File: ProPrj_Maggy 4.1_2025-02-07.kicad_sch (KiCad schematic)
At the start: 102 parts, among them CN1 430451000, CN2 0430450800, U1 LM1117S-5.0, U10 TLV493DA1B6HTSA2, U11 TLV493DA1B6HTSA2, U12 TLV493DA1B6HTSA2, U13 TLV493DA1B6HTSA2, U14 TLV493DA1B6HTSA2, U15 TLV493DA1B6HTSA2, U16 TLV493DA1B6HTSA2, U17 TLV493DA1B6HTSA2, U2 LM1117S-3.3, U20 A4950ELJTR-T, U21 A4950ELJTR-T, U22 A4950ELJTR-T, U23 A4950ELJTR-T, U27 BZT52C6V2, U3 CH224K, U30 INA214AIDCKR, U31 INA214AIDCKR, U32 INA214AIDCKR, U33 INA214AIDCKR, U4 X6511FV-24-C85D32, U40 TLV2372IDR, U5 X6511FV-24-C85D32, U50 XY308-2.54-2P, U51 XY308-2.54-2P, U52 XY308-2.54-2P, U53 XY308-2.54-2P, U6 XH-4AW米色, U7 TCA9548APWR

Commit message: feat: updated schematic with replacement from I2C sensors to SPI sensors
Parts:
- removed ?: (no value), ProPrj_Mag-easyedapro:, symbol ProPrj_Mag-easyedapro:Sheet-Symbol_A4
- removed C10, C11, C12, C13, C14, C5, C7, C8, C9: 100nF, ProPrj_Maggy 4.1_2025-02-07-import-fps:C0805, symbol ProPrj_Mag-easyedapro:CAP
- removed C6: 1uF, ProPrj_Maggy 4.1_2025-02-07-import-fps:C0805, symbol ProPrj_Mag-easyedapro:CAP
- removed R1, R2: 1k2, ProPrj_Maggy 4.1_2025-02-07-import-fps:R0805, symbol ProPrj_Mag-easyedapro:Res
- removed R10, R11, R12, R13, R14, R15, R16, R17, R18, R19, R20, R21, R6, R7, R8, R9: 1k2, ProPrj_Mag-easyedapro:, symbol ProPrj_Mag-easyedapro:Res
- removed U10, U11, U12, U13, U14, U15, U16, U17: TLV493DA1B6HTSA2, ProPrj_Mag-easyedapro:, symbol ProPrj_Mag-easyedapro:TLV493DA1B6HTSA2
- removed U6: XH-4AW米色, ProPrj_Mag-easyedapro:, symbol ProPrj_Mag-easyedapro:S4B-PH-KL(LF)(SN)
- removed U7: TCA9548APWR, ProPrj_Mag-easyedapro:, symbol ProPrj_Mag-easyedapro:PCA9548APW
- added C28, C29, C30, C31, C32: 100nF, ProPrj_Maggy 4.1_2025-02-07-import-fps:C0805, symbol ProPrj_Mag-easyedapro:CAP
- added R30, R31, R41: 10K, ProPrj_Mag-easyedapro:R0805, symbol ProPrj_Mag-easyedapro:Res
- added U18, U19, U7, U8, U9: TMAG5170A2DGKR, Package_SO:VSSOP-8_3x3mm_P0.65mm, symbol Sensor_Magnetic:TMAG5170-Q1
- R32, R33, R34: value 1k2 -> 10K; footprint ProPrj_Maggy 4.1_2025-02-07-import-fps:R0805 -> ProPrj_Mag-easyedapro:R0805; Check false -> (none)
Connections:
- net 3V3: no longer R32.1, R33.1, R34.1
- net GND: now also C28.1, C29.1, C30.1, C31.1, C32.1, U18.6 (GND), U18.7 (TEST), U19.6 (GND), U19.7 (TEST), U7.6 (GND), U7.7 (TEST), U8.6 (GND), U8.7 (TEST), U9.6 (GND), U9.7 (TEST)
- net SPI_SCLK: now reaches U5.14
- net SPI_SCLK: now also U18.1 (SCLK), U19.1 (SCLK), U7.1 (SCLK), U8.1 (SCLK), U9.1 (SCLK)
- net SPI_MOSI: now reaches U4.13
- net SPI_MOSI: now also U18.2 (MOSI), U19.2 (MOSI), U7.2 (MOSI), U8.2 (MOSI), U9.2 (MOSI)
- net SPI_MISO: now reaches U4.14
- net SPI_MISO: now also U18.3 (MISO), U19.3 (MISO), U7.3 (MISO), U8.3 (MISO), U9.3 (MISO)
- net SPI_CS_4: now reaches U4.19
- net SPI_CS_4: now also R33.1, U18.4 (~{CS})
- net SPI_CS_5: now reaches U4.20
- net SPI_CS_5: now also R34.1, U19.4 (~{CS})
- net TMAG_ALERT: now reaches U4.21
- net TMAG_ALERT: now also R41.2, U18.8 (~{ALERT}), U19.8 (~{ALERT}), U7.8 (~{ALERT}), U8.8 (~{ALERT}), U9.8 (~{ALERT})
- net I2C_RST renamed SPI_CS_3
- net SPI_CS_3: now also R32.1, U9.4 (~{CS}); no longer R32.2
- net I2C_SCL: no longer names the net of U5.8
- net I2C_SCL2 renamed SPI_CS_1
- net SPI_CS_1: now also R30.1, U7.4 (~{CS}); no longer R34.2
- net I2C_SDA: no longer names the net of U5.9
- net I2C_SDA2 renamed SPI_CS_2
- net SPI_CS_2: now also R31.1, U8.4 (~{CS}); no longer R33.2
- new net +3V3: R41.1
- new net VCC: C28.2, C29.2, C30.2, C31.2, C32.2, R30.2, R31.2, R32.2, R33.2, R34.2, U18.5 (VCC), U19.5 (VCC), U7.5 (VCC), U8.5 (VCC), U9.5 (VCC)
- no-connect marks 26 -> 22
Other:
- note removed: "Mux_Sensors"
- moved on the sheet: C1, C15, C16, C17, C18, C19, C2, C20, C21, C22, C23, C24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

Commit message: chore: replace EasyEDA power symbols with KiCad power symbols
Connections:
- net 3V3 is gone; now on net +3V3: C23.2, C24.2, C25.2, C26.2, C27.1, C4.1, LED1.2 (A), R27.1, R28.2, R39.2, U2.2 (OUT), U2.4 (TAB), U20.4 (VREF), U21.4 (VREF), U22.4 (VREF), U23.4 (VREF), U3.1 (VDD), U30.3 (V+), U31.3 (V+), U32.3 (V+), U33.3 (V+), U40.8 (VDD+)
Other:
- moved on the sheet: C24, C25, R36, U31

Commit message: chore: re-annotated entire schematic
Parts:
- renumbered C27 to C1, C2 to C10, C4 to C11, C22 to C12, C18 to C13, C23 to C14, C25 to C15, C24 to C16, C26 to C17, C28 to C18, C29 to C19, C15 to C2, C30 to C20, C31 to C21, C32 to C22, C19 to C3, C16 to C4, C20 to C5, C1 to C6, C3 to C7, C21 to C8, C17 to C9, CN2 to CN1, CN1 to CN2, LED4 to LED1, LED3 to LED2, LED2 to LED3, LED1 to LED4, R29 to R1, R25 to R10, R23 to R11, R4 to R12, R3 to R13, R41 to R14, R35 to R15, R37 to R16, R36 to R17, R38 to R18, R30 to R19, R26 to R2, R31 to R20, R32 to R21, R33 to R22, R34 to R23, R27 to R3, R22 to R4, R24 to R5, R28 to R6, R5 to R7, R39 to R8, R40 to R9, U20 to U1, U21 to U10, U1 to U11, U2 to U12, U40 to U13, U4 to U14, U30 to U15, U32 to U16, U5 to U17, U31 to U18, U33 to U19, U22 to U2, U7 to U20, U8 to U21, U9 to U22, U18 to U23, U19 to U24, U27 to U4, U50 to U5, U51 to U6, U52 to U7, U53 to U8, U23 to U9

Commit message: chore: auto-placed labels, replaced easyeda yellow-green LED with KiCad LED
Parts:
- LED1: value XL-1608SYGC-06 -> Yellow-Green; footprint ProPrj_Maggy 4.1_2025-02-07-import-fps:LED0603-RD_GREEN -> LED_SMD:LED_0603_1608Metric; symbol ProPrj_Mag-easyedapro:XL-1608SYGC-06 -> Device:LED
- LED2, LED4: footprint ProPrj_Maggy 4.1_2025-02-07-import-fps:LED0603-RD_GREEN -> ProPrj_Mag-easyedapro:LED0603-RD_GREEN; symbol ProPrj_Mag-easyedapro:XL-1608SYGC-06 -> Device:LED
- LED3: footprint ProPrj_Maggy 4.1_2025-02-07-import-fps:LED0603-RD_RED -> ProPrj_Mag-easyedapro:LED0603-RD_RED; symbol ProPrj_Mag-easyedapro:XL-1608SURC-06 -> Device:LED; LCSC Part Name XL-1608SYGC-06 -> XL-1608SURC-06; Manufacturer Part XL-1608SYGC-06 -> XL-1608SURC-06; Supplier Part C965805 -> C965799
- R1, R10, R11, R12, R13, R14, R19, R2, R20, R21, R22, R23, R3, R4, R5, R6, R7, R8, R9: symbol ProPrj_Mag-easyedapro:Res -> Device:R
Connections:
- net +3V3: no longer LED4.2 (A), R14.1
- net +5V: no longer LED3.2 (A)
- net TMAG_ALERT: no longer R14.2
- net at LED4.1 (K): no longer R13.2
- net at U4.1 (C): no longer LED2.1 (K)
- net at R7.1: no longer LED2.2 (A)
- net at R12.2: no longer LED3.1 (K)

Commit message: chore: replaced all yellow-green LEDs
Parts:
- LED2, LED4: value XL-1608SYGC-06 -> Yellow-Green; footprint ProPrj_Mag-easyedapro:LED0603-RD_GREEN -> LED_SMD:LED_0603_1608Metric
- LED3: value XL-1608SYGC-06 -> Yellow-Green; footprint ProPrj_Mag-easyedapro:LED0603-RD_RED -> LED_SMD:LED_0603_1608Metric
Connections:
- net +3V3: now also LED4.2 (A), R14.1
- net +5V: now also LED3.2 (A)
- net TMAG_ALERT: now also R14.2
- net at LED4.1 (K): now also R13.2
- net at U4.1 (C): now also LED2.1 (K)
- net at R7.1: now also LED2.2 (A)
- net at R12.2: now also LED3.1 (K)
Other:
- moved on the sheet: R14
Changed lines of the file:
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@@
 	(wire
 		(pts
-			(xy 179.07 82.55) (xy 179.07 81.28)
-		)
-		(stroke
-			(width 0)
-			(type default)
-		)
-	)
-	(wire
-		(pts
 			(xy 339.09 97.79) (xy 341.63 97.79)
 		)
@@
 	(wire
 		(pts
-			(xy 179.07 71.12) (xy 179.07 69.85)
-		)
-		(stroke
-			(width 0)
-			(type default)
-		)
-	)
-	(wire
-		(pts
 			(xy 124.46 273.05) (xy 121.92 273.05)
 		)
@@
 	(wire
 		(pts
-			(xy 179.07 46.99) (xy 179.07 48.26)
+			(xy 179.07 45.72) (xy 179.07 48.26)
 		)
 		(stroke
@@
 	(wire
 		(pts
-			(xy 179.07 36.83) (xy 179.07 35.56)
+			(xy 179.07 35.56) (xy 179.07 38.1)
 		)
 		(stroke
@@
 	(wire
 		(pts
-			(xy 102.87 161.29) (xy 102.87 162.56)
+			(xy 102.87 161.29) (xy 102.87 163.83)
 		)
 		(stroke
@@
 	(wire
 		(pts
+			(xy 179.07 69.85) (xy 179.07 72.39)
+		)
+		(stroke
+			(width 0)
+			(type default)
+		)
+	)
+	(wire
+		(pts
 			(xy 335.28 240.03) (xy 336.55 240.03)
 		)
@@
 	(wire
 		(pts
-			(xy 191.77 173.99) (xy 194.31 173.99)
+			(xy 191.77 173.99) (xy 195.58 173.99)
 		)
 		(stroke
@@
 	(wire
 		(pts
+			(xy 102.87 171.45) (xy 102.87 172.72)
+		)
+		(stroke
+			(width 0)
+			(type default)
+		)
+	)
+	(wire
+		(pts
 			(xy 354.33 196.85) (xy 359.41 196.85)
 		)
@@
 	(wire
 		(pts
+			(xy 179.07 80.01) (xy 179.07 82.55)
+		)
+		(stroke
+			(width 0)
+			(type default)
+		)
+	)
+	(wire
+		(pts
 			(xy 142.24 186.69) (xy 152.4 186.69)
 		)
@@
 	(wire
 		(pts
+			(xy 203.2 173.99) (xy 204.47 173.99)
+		)
+		(stroke
+			(width 0)
+			(type default)
+		)
+	)
+	(wire
+		(pts
 			(xy 130.81 82.55) (xy 130.81 74.93)
 		)
@@
 		(at 179.07 76.2 90)
 		(unit 1)
-		(body_style 0)
+		(body_style 1)
 		(exclude_from_sim no)
 		(in_bom yes)
@@
 			)
 		)
-		(property "Value" "XL-1608SYGC-06"
+		(property "Value" "Yellow-Green"
 			(at 182.88 79.0574 90)
 			(show_name no)
@@
 			)
 		)
-		(property "Footprint" "ProPrj_Mag-easyedapro:LED0603-RD_GREEN"
+		(property "Footprint" "LED_SMD:LED_0603_1608Metric"
 			(at 179.07 76.2 0)
 			(hide yes)
@@
 			)
 		)
-		(property "Value" "XL-1608SYGC-06"
+		(property "Value" "Yellow-Green"
 			(at 106.68 170.4974 90)
 			(show_name no)
@@
 			)
 		)
-		(property "Footprint" "ProPrj_Mag-easyedapro:LED0603-RD_GREEN"
+		(property "Footprint" "LED_SMD:LED_0603_1608Metric"
 			(at 102.87 167.64 0)
 			(hide yes)
@@
 		(at 179.07 41.91 90)
 		(unit 1)
-		(body_style 0)
+		(body_style 1)
 		(exclude_from_sim no)
 		(in_bom yes)
@@
 			)
 		)
-		(property "Value" "XL-1608SYGC-06"
+		(property "Value" "Yellow-Green"
 			(at 182.88 44.7674 90)
 			(show_name no)
@@
 			)
 		)
-		(property "Footprint" "ProPrj_Mag-easyedapro:LED0603-RD_RED"
+		(property "Footprint" "LED_SMD:LED_0603_1608Metric"
 			(at 179.07 41.91 0)
 			(hide yes)
@@
 	(symbol
 		(lib_id "Device:R")
-		(at 199.39 173.99 0)
+		(at 199.39 173.99 90)
 		(unit 1)
 		(body_style 1)
@@
 		(fields_autoplaced yes)
 		(property "Reference" "R14"
-			(at 201.93 172.7199 0)
+			(at 199.39 167.64 90)
 			(show_name no)
 			(do_not_autoplace no)
@@
 					(size 1.27 1.27)
 				)
-				(justify left)
 			)
 		)
 		(property "Value" "10K"
-			(at 201.93 175.2599 0)
+			(at 199.39 170.18 90)
 			(show_name no)
 			(do_not_autoplace no)
@@
 					(size 1.27 1.27)
 				)
-				(justify left)
 			)
 		)

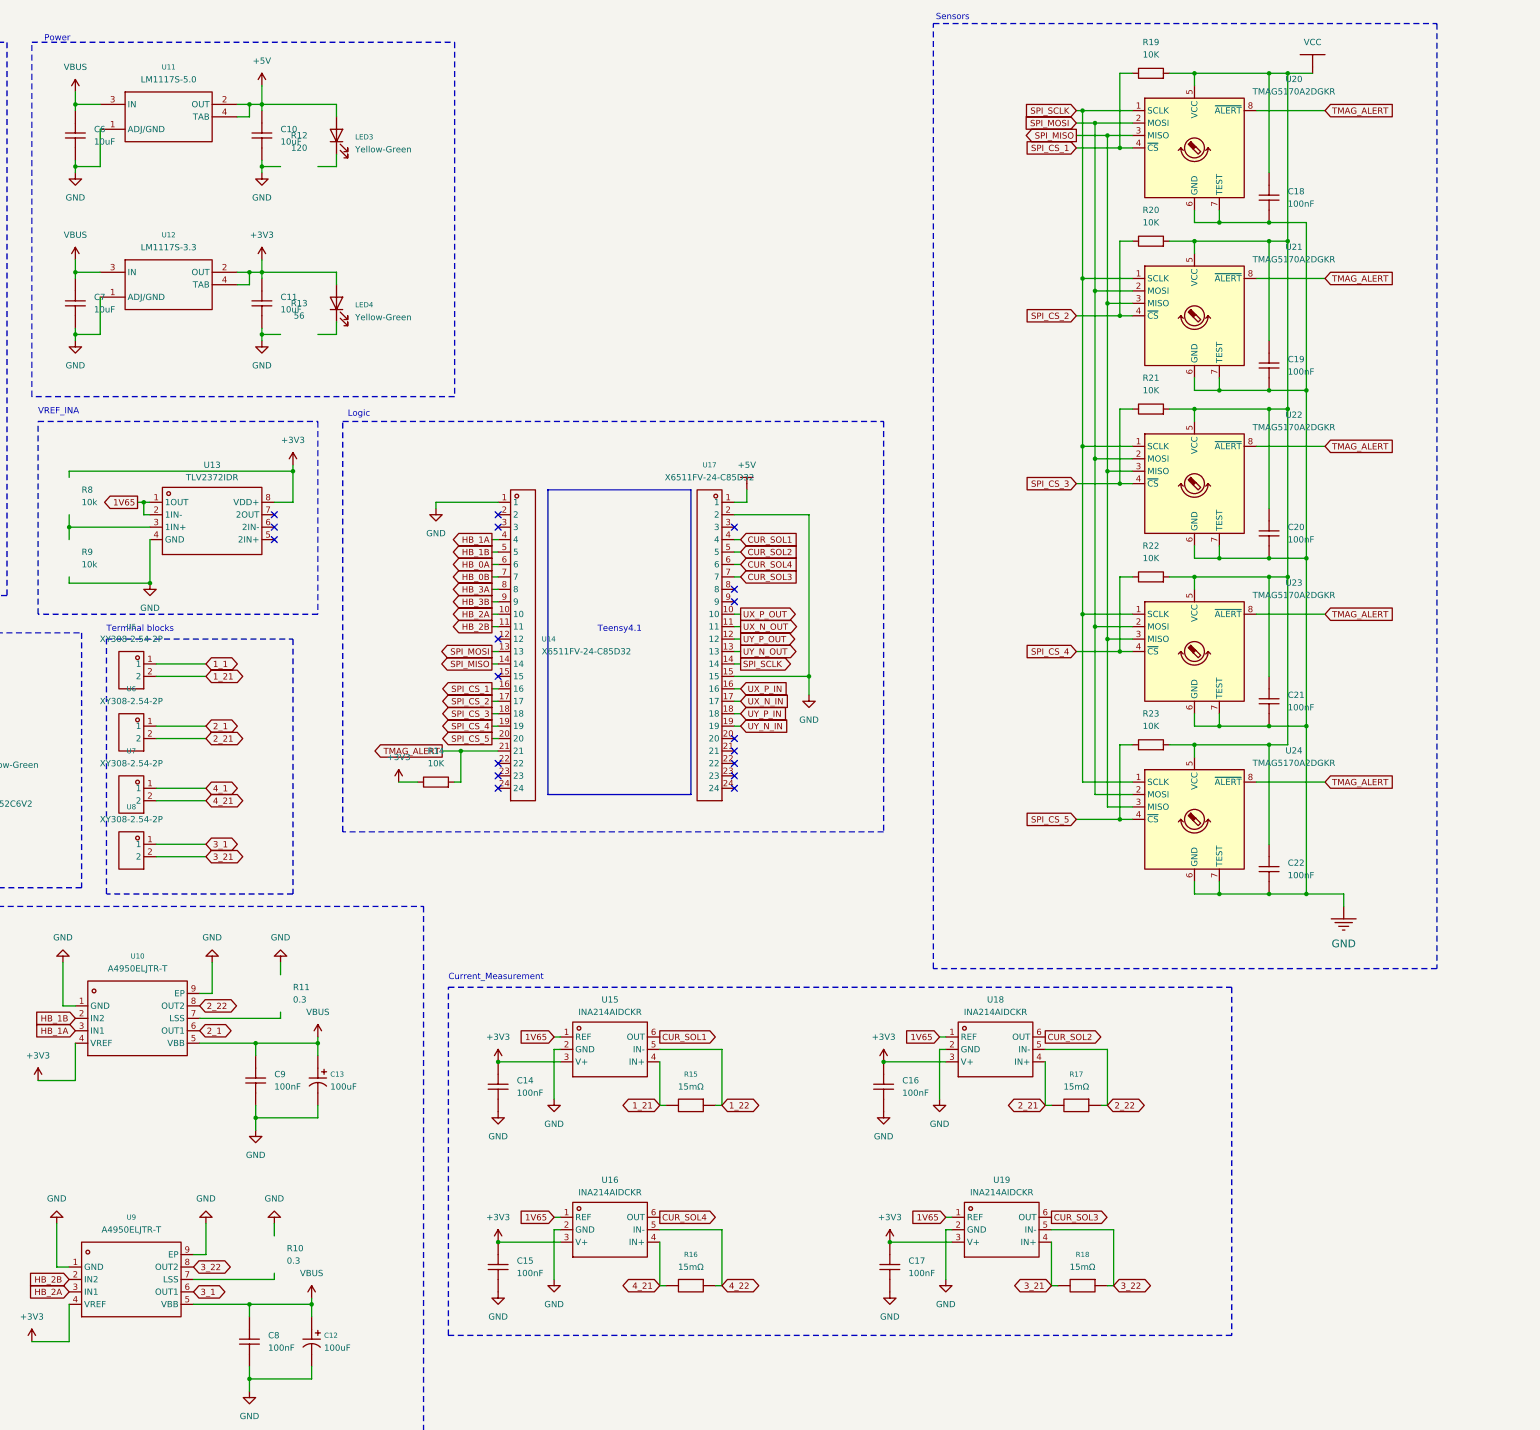
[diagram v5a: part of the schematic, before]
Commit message: feat: added teensy 4.1 to schematic
Added the Teensy 4.1 symbol to the libs/ directory, and replaced the old symbol in the schematic using two female headers with the new symbol, which gives correct pin directions, descriptions, etc.
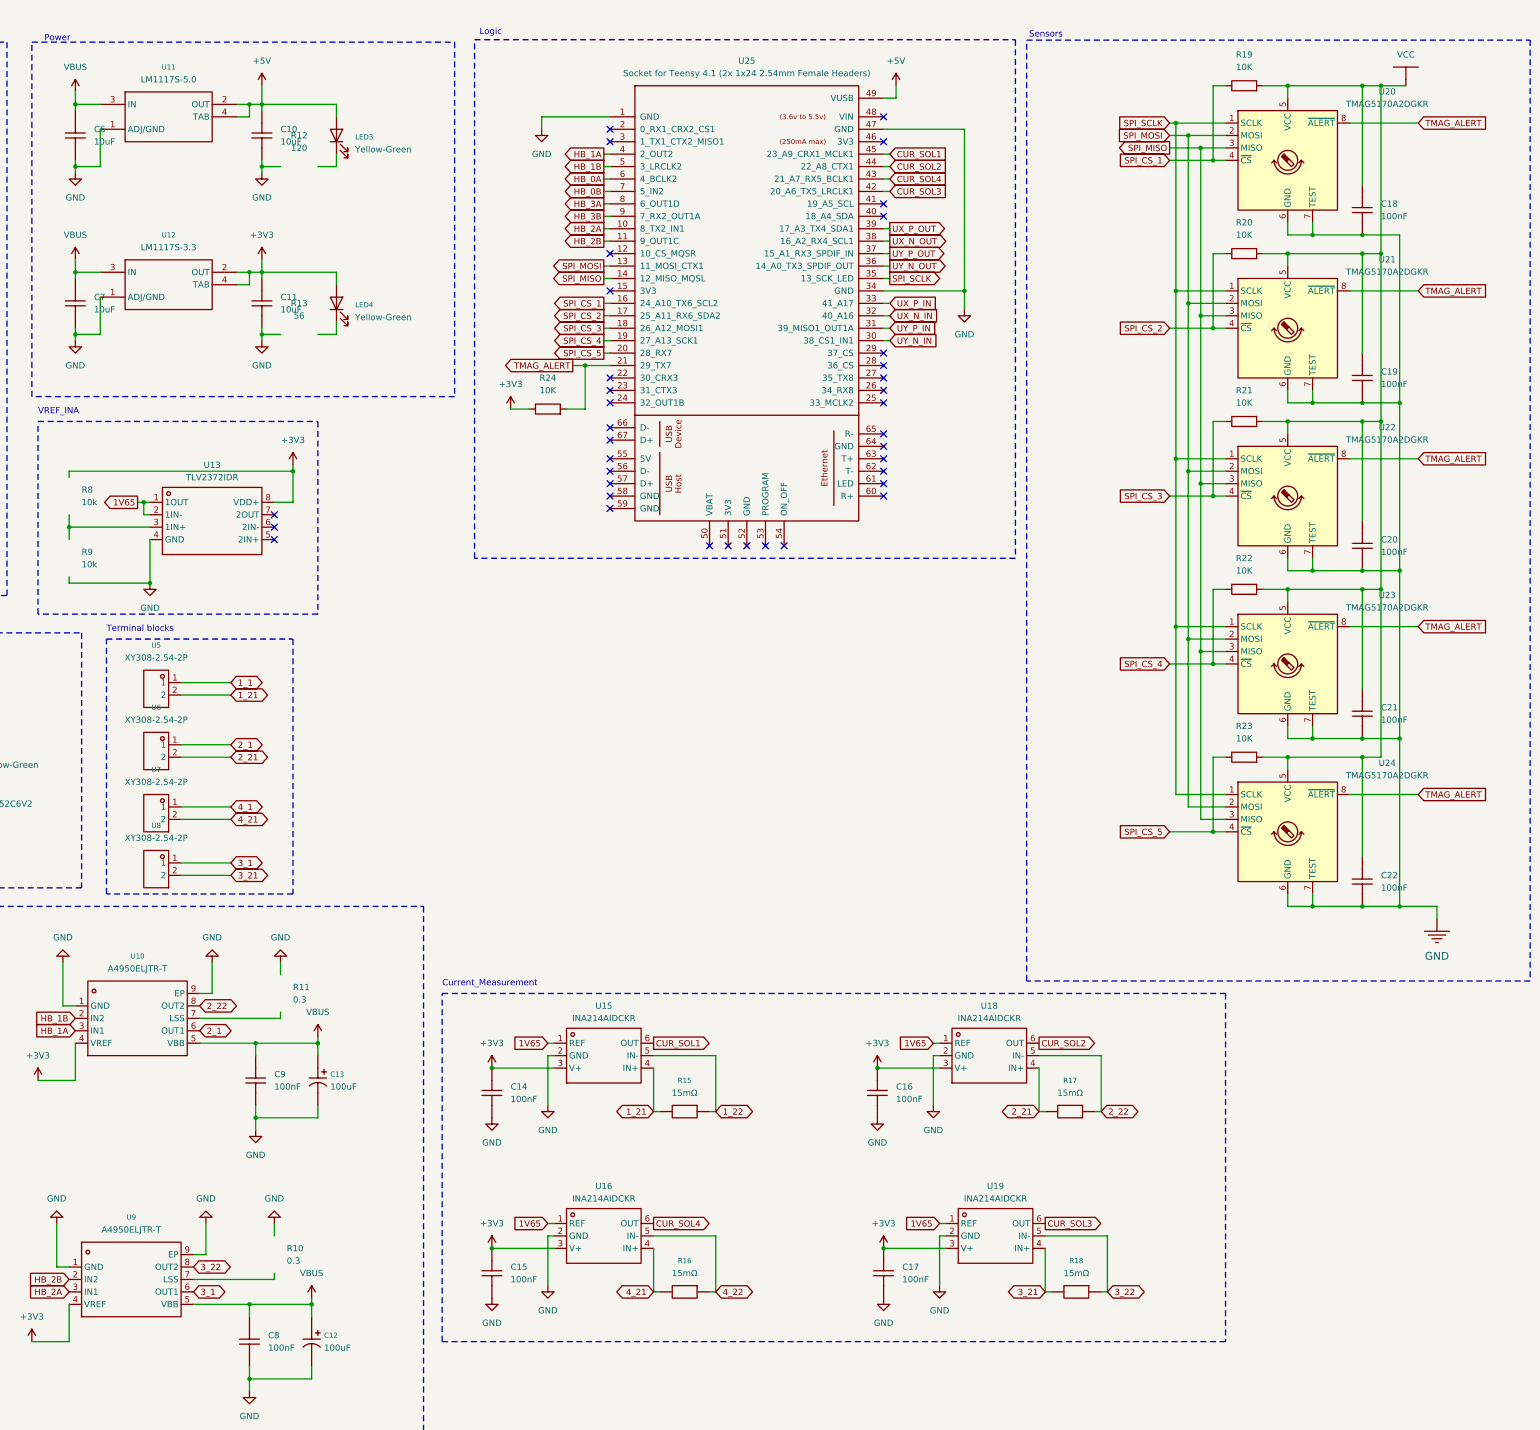
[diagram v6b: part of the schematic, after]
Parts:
- removed R14: 10K, ProPrj_Mag-easyedapro:R0805, symbol Device:R
- removed U14, U17: X6511FV-24-C85D32, ProPrj_Maggy 4.1_2025-02-07-import-fps:HDR-TH_24P-P2.54-V-F, symbol ProPrj_Mag-easyedapro:X6511FV-24-C85D32
- added R24: 10K, ProPrj_Mag-easyedapro:R0805, symbol Device:R
- added U25: Socket for Teensy 4.1 (2x 1x24 2.54mm Female Head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, symbol teensy:Teensy4.1
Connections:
- net +3V3: now also R24.1
- net +5V: now also U25.49 (VUSB)
- net CUR_SOL1: now also U25.45 (23_A9_CRX1_MCLK1)
- net CUR_SOL2: now also U25.44 (22_A8_CTX1)
- net CUR_SOL3: now also U25.42 (20_A6_TX5_LRCLK1)
- net CUR_SOL4: now also U25.43 (21_A7_RX5_BCLK1)
- net GND: now also U25.1 (GND), U25.34 (GND), U25.47 (GND)
- net HB_0A: now also U25.6 (4_BCLK2)
- net HB_0B: now also U25.7 (5_IN2)
- net HB_1A: now also U25.4 (2_OUT2)
- net HB_1B: now also U25.5 (3_LRCLK2)
- net HB_2A: now also U25.10 (8_TX2_IN1)
- net HB_2B: now also U25.11 (9_OUT1C)
- net HB_3A: now also U25.8 (6_OUT1D)
- net HB_3B: now also U25.9 (7_RX2_OUT1A)
- net SPI_CS_1: now also U25.16 (24_A10_TX6_SCL2)
- net SPI_CS_2: now also U25.17 (25_A11_RX6_SDA2)
- net SPI_CS_3: now also U25.18 (26_A12_MOSI1)
- net SPI_CS_4: now also U25.19 (27_A13_SCK1)
- net SPI_CS_5: now also U25.20 (28_RX7)
- net SPI_MISO: now also U25.14 (12_MISO_MQSL)
- net SPI_MOSI: now also U25.13 (11_MOSI_CTX1)
- net SPI_SCLK: now also U25.35 (13_SCK_LED)
- net TMAG_ALERT: now also R24.2, U25.21 (29_TX7)
- net UX_N_IN: now also U25.32 (40_A16)
- net UX_N_OUT: now also U25.38 (16_A2_RX4_SCL1)
- net UX_P_IN: now also U25.33 (41_A17)
- net UX_P_OUT: now also U25.39 (17_A3_TX4_SDA1)
- net UY_N_IN: now also U25.30 (38_CS1_IN1)
- net UY_N_OUT: now also U25.36 (14_A0_TX3_SPDIF_OUT)
- net UY_P_IN: now also U25.31 (39_MISO1_OUT1A)
- net UY_P_OUT: now also U25.37 (15_A1_RX3_SPDIF_IN)
- no-connect marks 22 -> 41
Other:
- note removed: "Teensy4.1"
- moved on the sheet: C14, C15, C16, C17, C18, C19, C20, C21, C22, R15, R16, R17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
